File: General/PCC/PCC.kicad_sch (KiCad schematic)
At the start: 23 parts, among them J1 Conn_01x03, SW1 SW_DIP_x04, U1 I6A4W020A033V-001-R

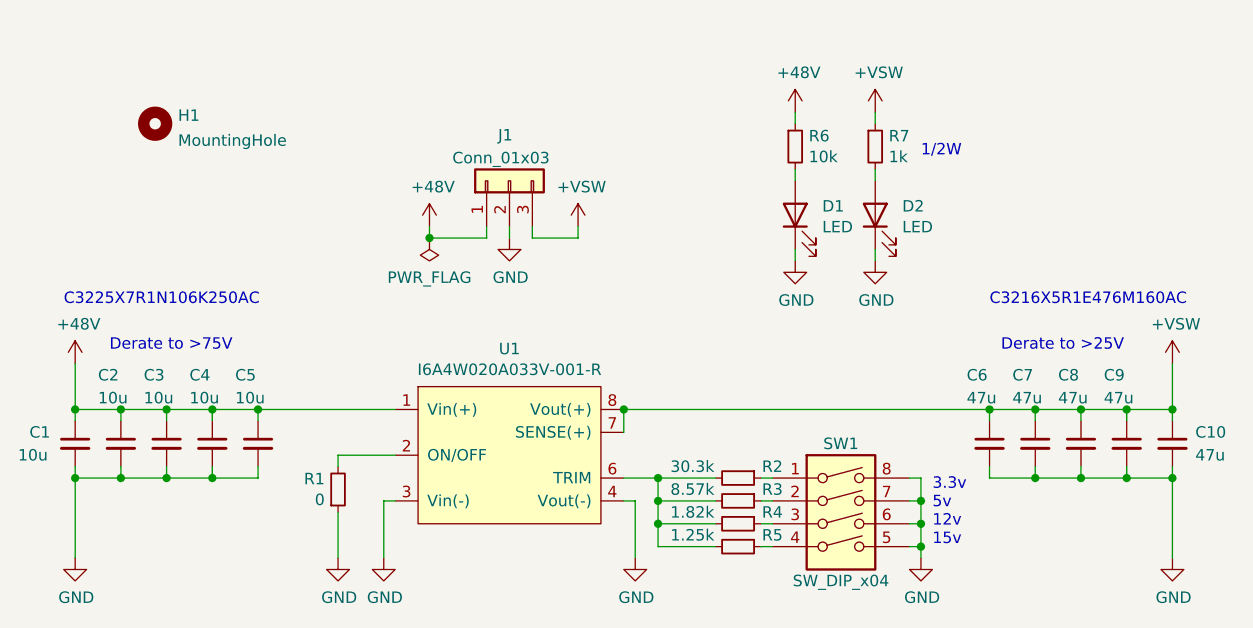
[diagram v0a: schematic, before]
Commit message: updated layout
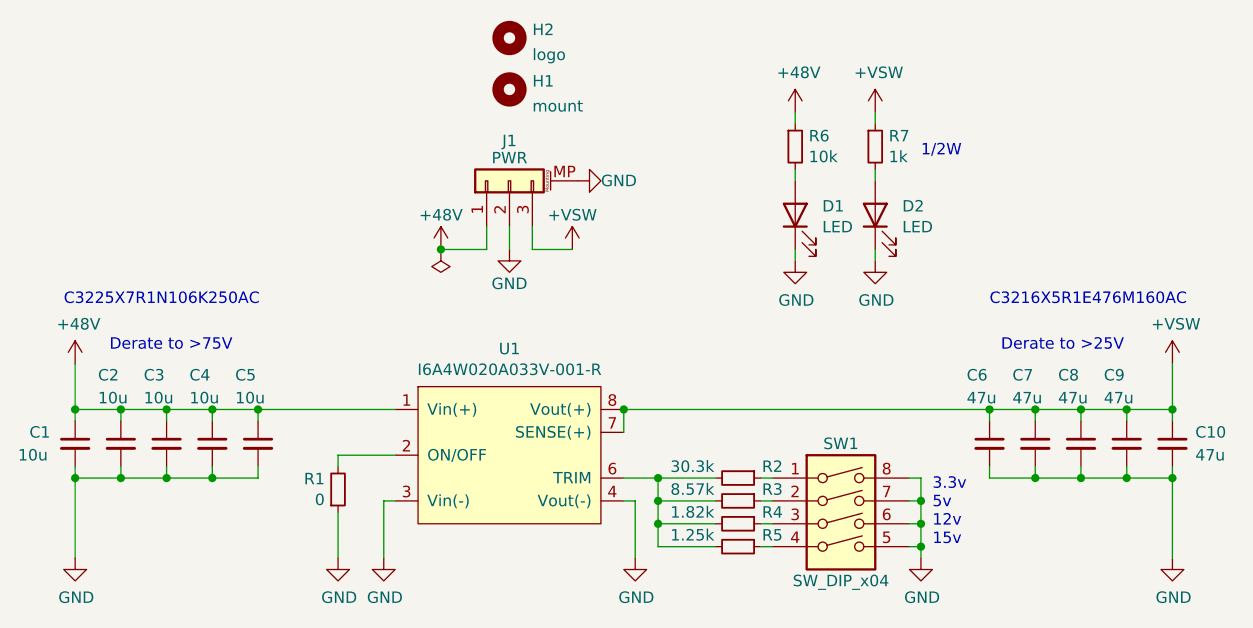
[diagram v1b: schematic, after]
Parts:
- removed J1: Conn_01x03, extraparts:Samtec_mPOWER_UMPT_3pin, symbol Connector_Generic:Conn_01x03
- added H2: logo, extraparts:auv_logo, symbol Mechanical:MountingHole
- added J1: PWR, extraparts:Samtec_mPOWER_UMPT_3pin, symbol Connector_Generic_MountingPin:Conn_01x03_MountingPin
- H1: value MountingHole -> mount; footprint MountingHole:MountingHole_3.2mm_M3 -> MountingHole:MountingHole_3.2mm_M3_Pad_TopBottom
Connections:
- net +48V: now also J1.1 (Pin_1)
- net +VSW: now also J1.3 (Pin_3)
- net GND: now also J1.2 (Pin_2), J1.MP (MountPin)
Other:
- moved on the sheet: H1
